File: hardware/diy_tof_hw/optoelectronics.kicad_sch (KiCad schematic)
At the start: 39 parts, among them IC21 74LVC1G08QW5-7, IC22 LMG1025QDEETQ1, SW2 SW_Nidec_CAS-120A1, U2 OPA858xDSG, U3 TLV3501AIDBV

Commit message: [hardware/minor] added title for optoelectronics schematic page
Signed-off-by: Timon Burkard <burkard.timon@gmail.com>
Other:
- title: (none) -> Optoelectronics
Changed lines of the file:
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@@
 	(paper "A3")
 	(title_block
+		(title "Optoelectronics")
 		(rev "0.1")
 		(comment 2 "schematics")

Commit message: [hardware] initial version of the PCB layout
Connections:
- net at LD1.1, V1.5, V1.6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: now also V1.9
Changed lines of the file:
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@@
 	(wire
 		(pts
+			(xy 186.69 76.2) (xy 186.69 72.39)
+		)
+		(stroke
+			(width 0)
+			(type default)
+		)
+	)
+	(wire
+		(pts
 			(xy 78.74 156.21) (xy 86.36 156.21)
 		)
@@
 	(wire
 		(pts
+			(xy 186.69 72.39) (xy 189.23 72.39)
+		)
+		(stroke
+			(width 0)
+			(type default)
+		)
+	)
+	(wire
+		(pts
 			(xy 191.77 93.98) (xy 189.23 93.98)
 		)
@@
 		(pin "4"
 		)
+		(pin "9"
+		)
 		(instances

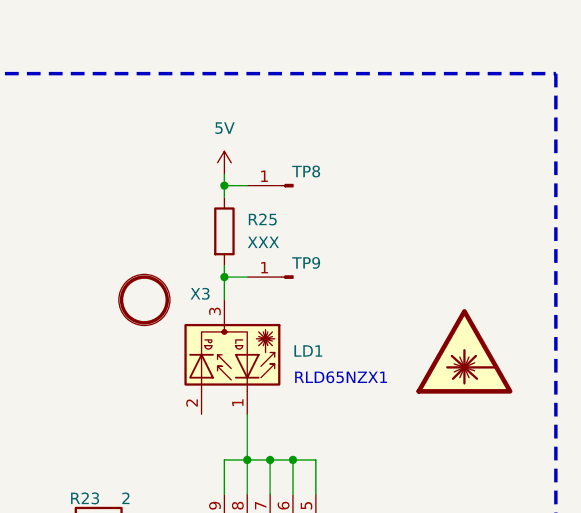
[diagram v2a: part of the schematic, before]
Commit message: [hardware] changed footprint of R25 to 0603, updated some ICs footprint models in order to comply with e.g. via hole size constraints
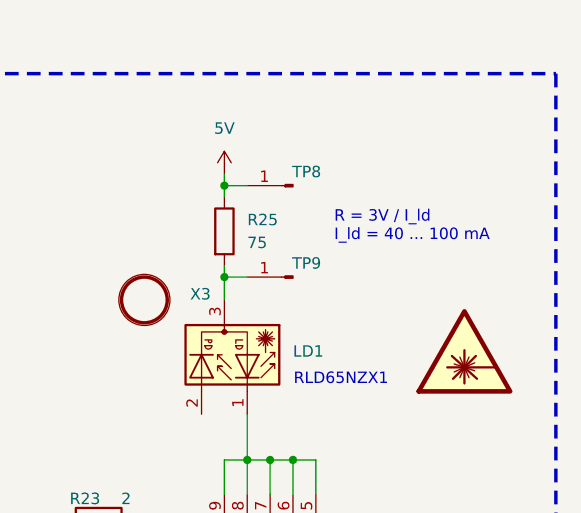
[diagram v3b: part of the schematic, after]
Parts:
- R25: value XXX -> 75; footprint Resistor_SMD:R_4020_10251Metric -> Resistor_SMD:R_0603_1608Metric_Pad0.98x0.95mm_HandSolder
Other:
- note added: "R = 3V / I_ld I_ld = 40 ... 100 mA"
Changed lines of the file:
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@@
 		)
 	)
+	(text "R = 3V / I_ld\nI_ld = 40 ... 100 mA"
+		(exclude_from_sim no)
+		(at 198.882 46.482 0)
+		(effects
+			(font
+				(size 1.27 1.27)
+			)
+			(justify left)
+		)
+	)
 	(text "Tp equals ~tau \n     -> 0.5 ... 100 ns"
 		(exclude_from_sim no)
@@
 			)
 		)
-		(property "Value" "XXX"
+		(property "Value" "75"
 			(at 189.23 48.2599 0)
 			(effects
@@
 			)
 		)
-		(property "Footprint" "Resistor_SMD:R_4020_10251Metric"
+		(property "Footprint" "Resistor_SMD:R_0603_1608Metric_Pad0.98x0.95mm_HandSolder"
 			(at 184.912 46.99 90)
 			(effects

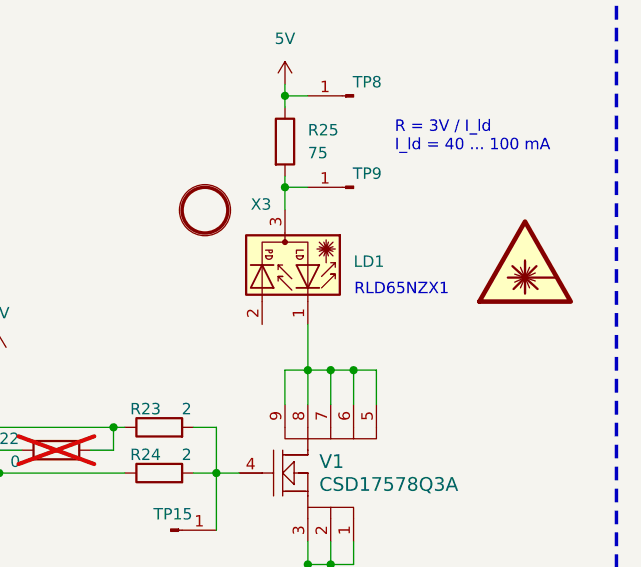
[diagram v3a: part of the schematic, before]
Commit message: [hardware] further review findings  - adjusted some more traces  - one via per power pad  - added caps for a pi filter (dnp)  - added pullups for the CS signals of both TDCs
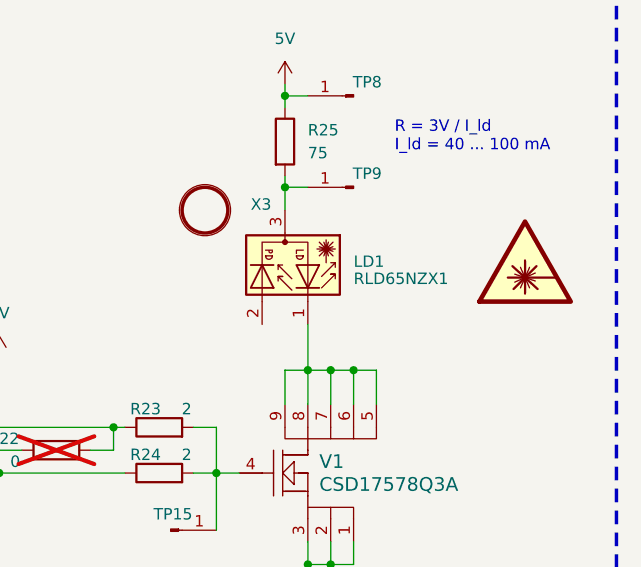
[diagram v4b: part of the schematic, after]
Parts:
- LD1: value ~ -> RLD65NZX1
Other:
- note removed: "RLD65NZX1"
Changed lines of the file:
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@@
-		)
-	)
-	(text "RLD65NZX1"
-		(exclude_from_sim no)
-		(at 199.644 63.5 0)
-		(effects
-			(font
-				(size 1.27 1.27)
-			)
 		)
 	)
@@
 			)
 		)
-		(property "Value" "~"
+		(property "Value" "RLD65NZX1"
 			(at 194.31 62.23 90)
 			(effects

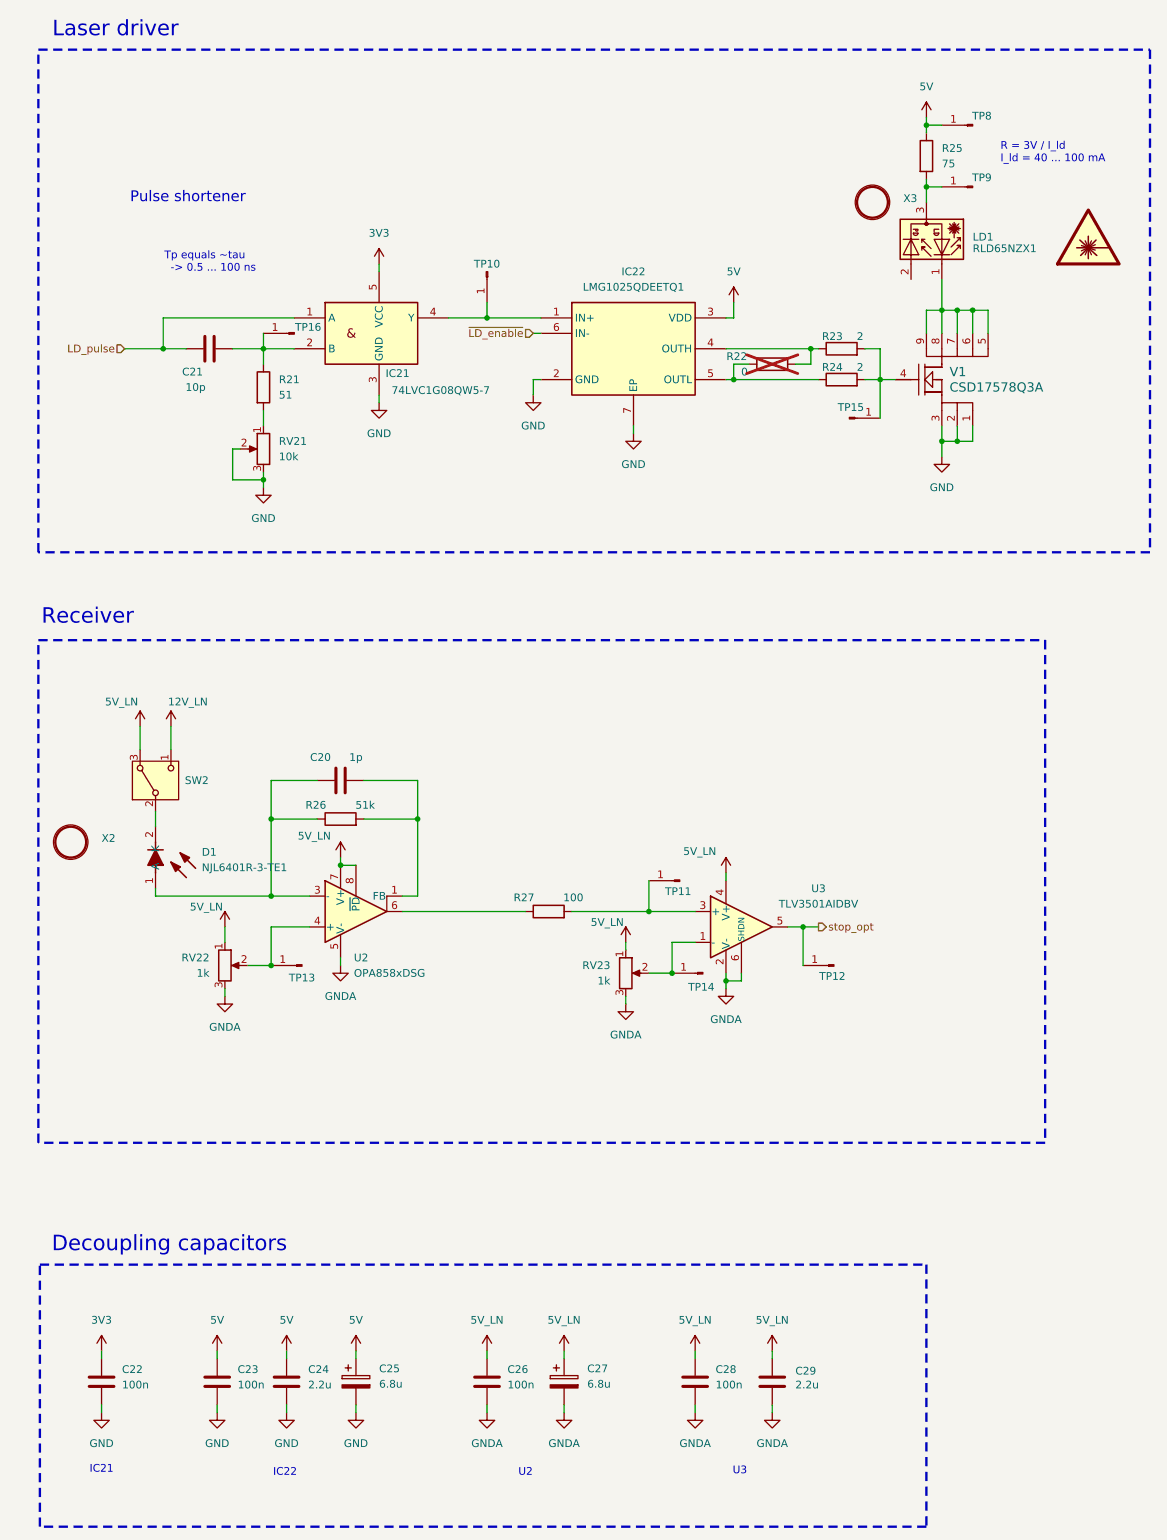
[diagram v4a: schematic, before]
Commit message: [hardware/minor] add value for optic mountings
Signed-off-by: Timon Burkard <burkard.timon@gmail.com>
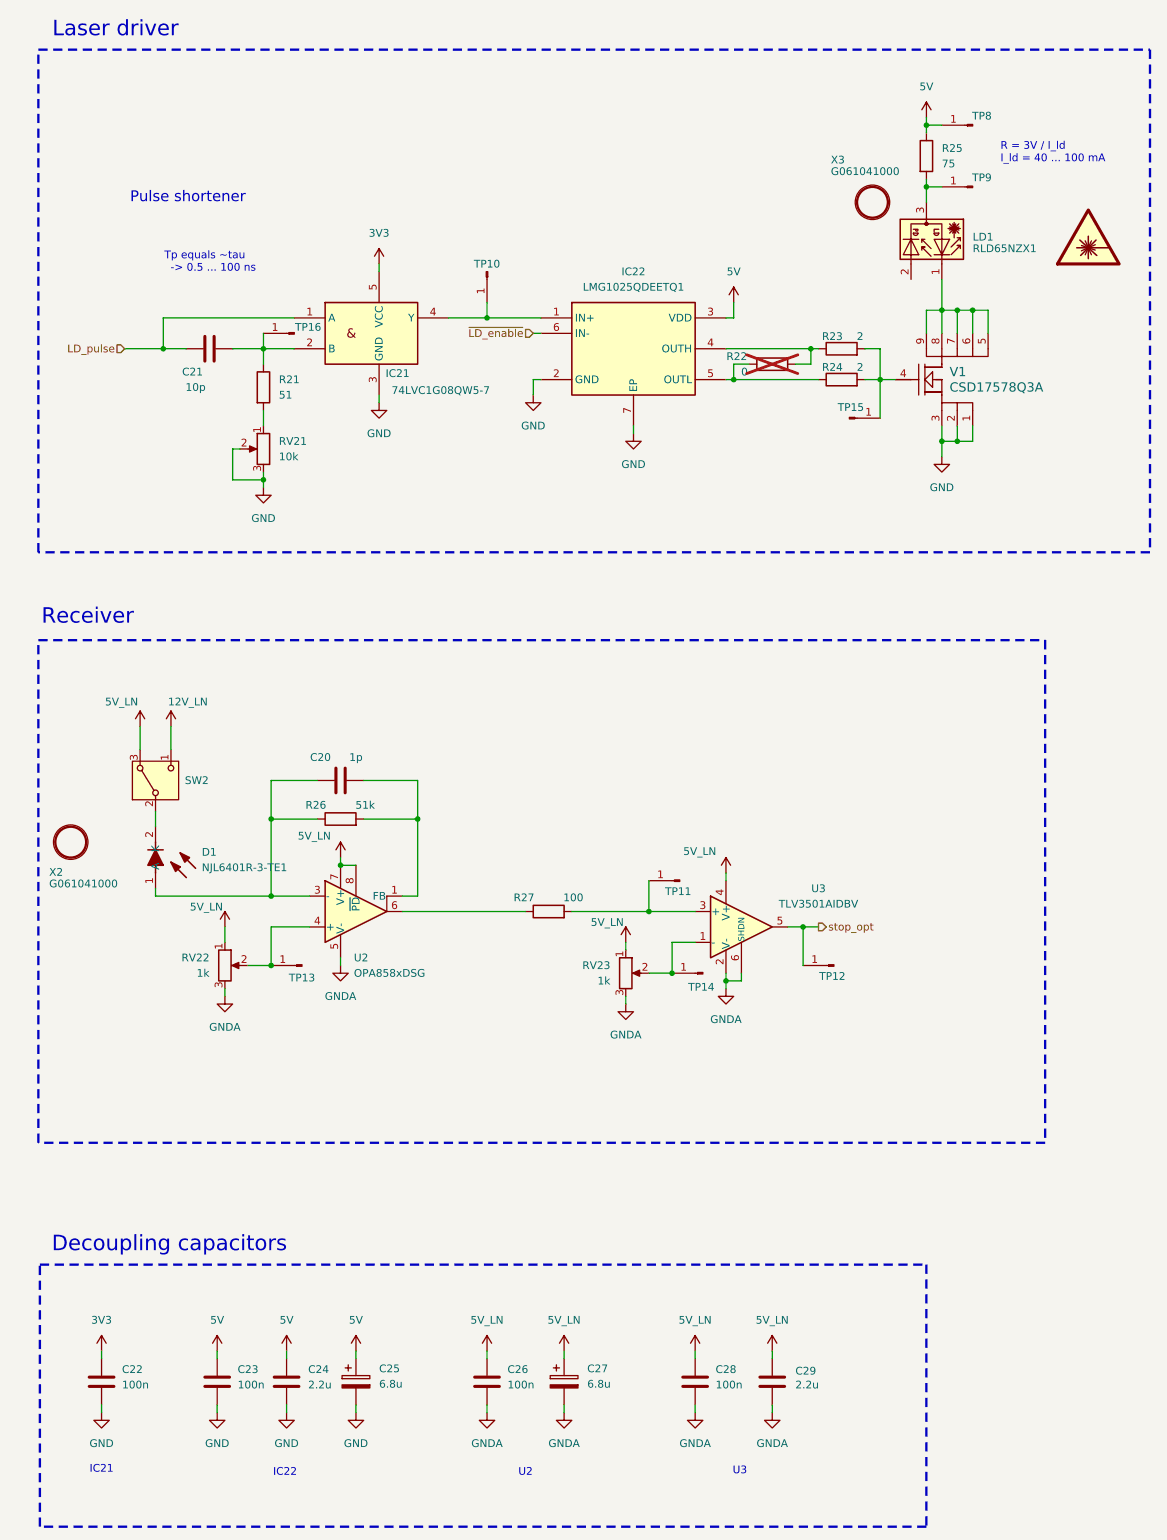
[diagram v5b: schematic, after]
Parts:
- X2, X3: value ~ -> G061041000
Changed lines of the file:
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@@
 		(on_board yes)
 		(dnp no)
-		(fields_autoplaced yes)
 		(property "Reference" "X2"
-			(at 50.8 159.3849 0)
+			(at 42.164 164.9729 0)
 			(effects
 				(font
@@
 			)
 		)
-		(property "Value" "~"
-			(at 50.8 161.29 0)
+		(property "Value" "G061041000"
+			(at 42.164 166.878 0)
 			(effects
 				(font
@@
 		(on_board yes)
 		(dnp no)
-		(fields_autoplaced yes)
 		(property "Reference" "X3"
-			(at 182.88 53.9749 0)
+			(at 170.942 47.6249 0)
 			(effects
 				(font
@@
 			)
 		)
-		(property "Value" "~"
-			(at 182.88 55.88 0)
-			(effects
-				(font
+		(property "Value" "G061041000"
+			(at 170.942 49.53 0)
+			(effects
+				(font

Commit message: [hardware] release v1.0
Signed-off-by: Timon Burkard <burkard.timon@gmail.com>
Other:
- company: (none) -> OST
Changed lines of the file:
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@@
 	(title_block
 		(title "Optoelectronics")
-		(rev "0.1")
+		(date "2024-12-27")
+		(rev "1.0")
+		(company "OST")
 		(comment 2 "schematics")
-		(comment 3 "w.i.p.")
+		(comment 3 "released")
 		(comment 8 "M. Schär")
+		(comment 9 "T. Burkard")
 	)
 	(junction
